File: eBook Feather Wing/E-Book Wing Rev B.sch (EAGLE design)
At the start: 92 parts, among them IC1 MCP23008/SO, IC2 23K256-I/SN, J1 MJ-3502N, Q1 IRLML0100, Q2 BSS138, Q3 DMG3415, SW1 SPDT_SWITCH

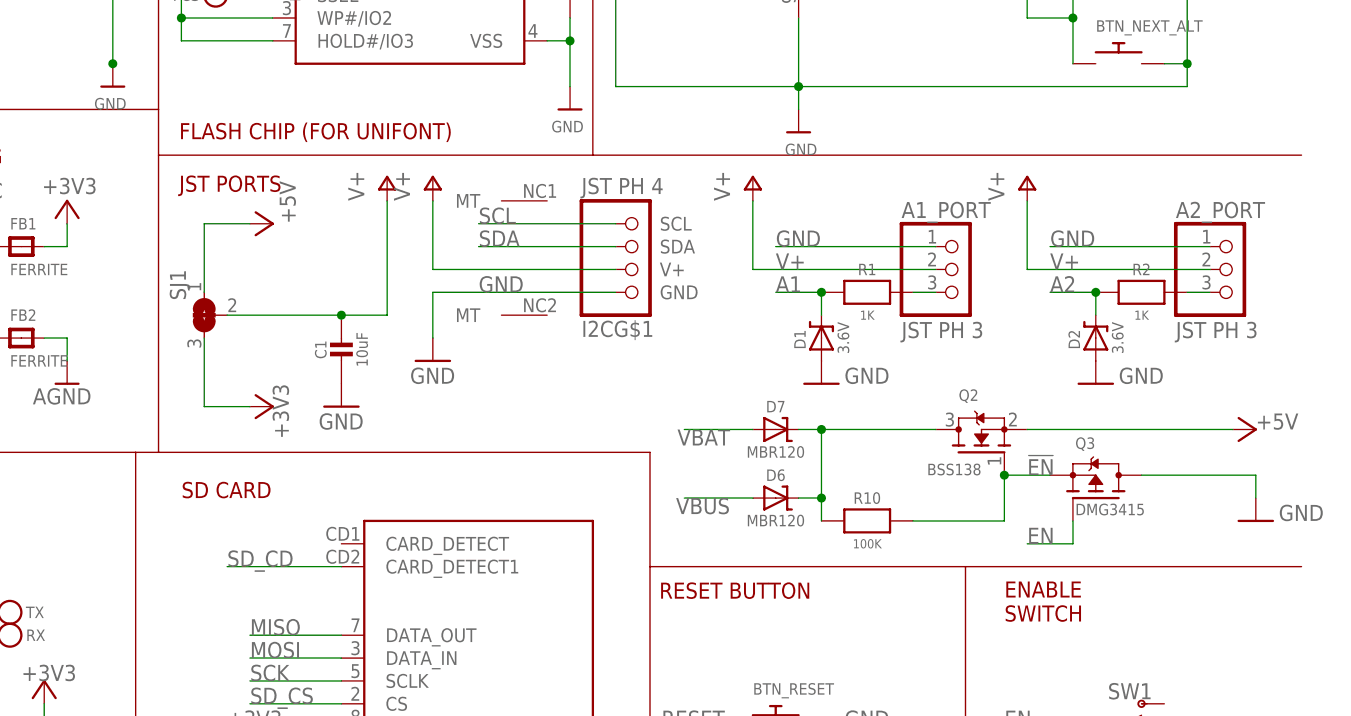
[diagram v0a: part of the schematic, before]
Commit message: remove 5V option, more complicated than I thought
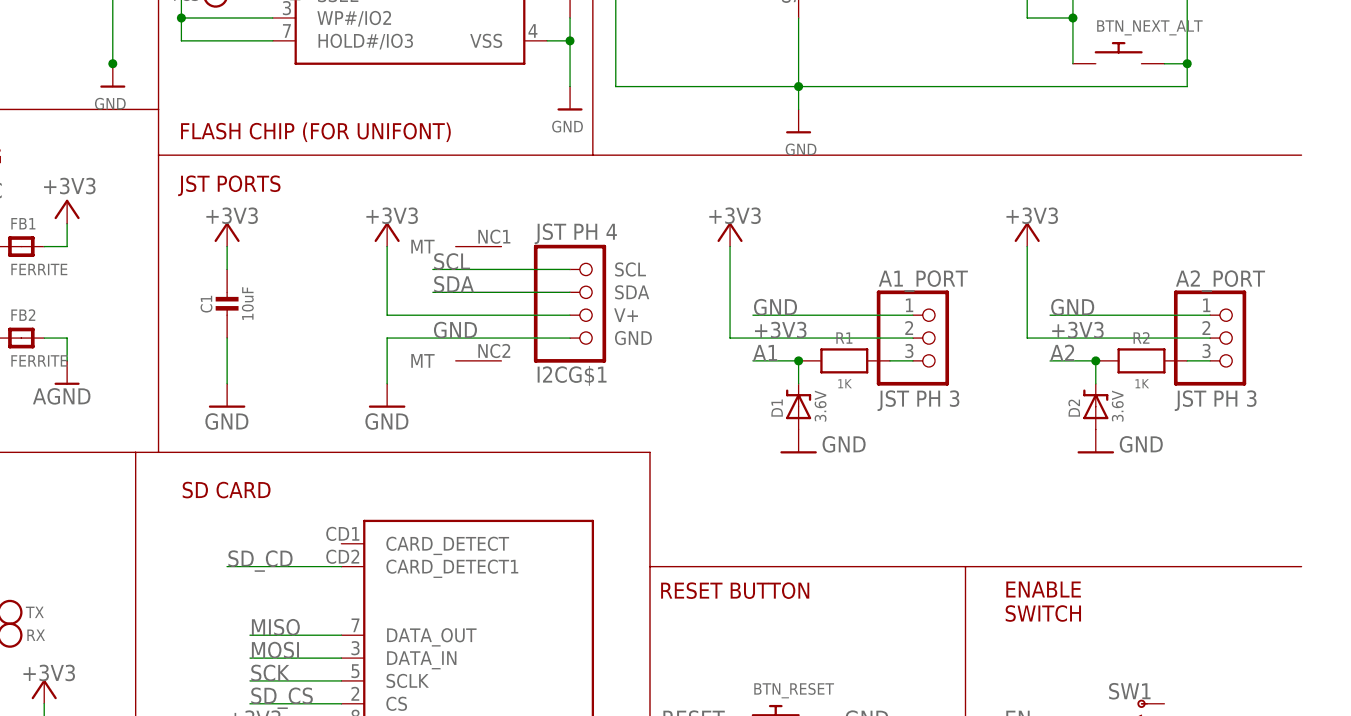
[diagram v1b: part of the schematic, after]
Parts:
- removed D6, D7: MBR120, microbuilder:DIODE-SCHOTTKYSOD-123
- removed Q2: BSS138, pygamer-microbuilder:MOSFET-NREFLOW
- removed Q3: DMG3415, pygamer-microbuilder:MOSFET-P
- removed R10: 100K, microbuilder:RESISTOR_0805MP
- removed SJ1: (no value), pygamer-microbuilder:SOLDERJUMPER_2WAY
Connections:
- removed net !EN: Q2.G, Q3.S, R10.1
- removed net +5V: Q2.S, SJ1.1
- removed net N$7: D6.C, D7.C, Q2.D, R10.2
- removed net V+: A1_PORT.2, A2_PORT.2, C1.1, I2CG$1.V+, SJ1.2
- net +3V3: now also A1_PORT.2, A2_PORT.2, C1.1, I2CG$1.V+; no longer SJ1.3
- net EN: no longer Q3.G
- net GND: no longer Q3.D
- net VBAT: no longer D7.A
- net VBUS: no longer D6.A
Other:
- moved on the sheet: A1_PORT, A2_PORT, C1, D1, D2, I2CG$1, R1, R2

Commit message: final commit of rev B as submitted to OSH Park
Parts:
- added BTN_LOCK: SPST_TACTILE_SWITCHRA, My Stuff:SPST_TACTILE_SWITCHRA
- added FID1, FID2, FID3, FID4: FIDUCIAL_1MM, microbuilder:FIDUCIAL_1MM
- added JP2: (no value), adafruit:PINHD-1X1
- added U$1, U$4, U$5, U$7: MOUNTINGHOLE2.5, microbuilder:MOUNTINGHOLE2.5
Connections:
- new net BTN_LOCK: BTN_LOCK.P$1, IC1.GP7
- net +3V3: now also JP2.1
- net GND: now also BTN_LOCK.P$2
- net SD_CD: no longer IC1.GP7
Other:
- moved on the sheet: A1_PORT, A2_PORT, C1, D1, D2, I2CG$1, R1, R2

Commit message: final tweaks and BOM for rev B
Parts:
- L1: value 68uH -> 10uH
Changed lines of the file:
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@@
 <part name="C9" library="microbuilder" deviceset="CAP_CERAMIC" device="0805-NOOUTLINE" value="4.7uF/25V"/>
 <part name="D3" library="microbuilder" deviceset="DIODE-SCHOTTKY" device="SOD-123" value="MBR0530"/>
-<part name="L1" library="microbuilder" deviceset="INDUCTOR" device="NR401" value="68uH"/>
+<part name="L1" library="microbuilder" deviceset="INDUCTOR" device="NR401" value="10uH"/>
 <part name="R5" library="microbuilder" deviceset="RESISTOR" device="0805_10MGAP" value="0.47ohm"/>
 <part name="U$10" library="microbuilder" deviceset="GND" device=""/>
